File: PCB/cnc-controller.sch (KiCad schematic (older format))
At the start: 12 parts

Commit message: キーマトリクスとLEDの回路図を作成
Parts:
- added R?: 10k, symbol Device:R
- added R?: 500, symbol Device:R
- added SW? (x24): sw_unit, symbol cnc-controller_Library:kailh_chocv1_sw_unit
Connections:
- net labels added: +5VP
- wire segments 65 -> 280
- no-connect marks 12 -> 13
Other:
- moved on the sheet: F?, J?, R?, U?

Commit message: USBのデータ線の保護素子を変更 USB周りの配線を変更及び書き直し
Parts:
- removed D? (x2): 5.1V, symbol Device:D_Zener
- removed R? (x2): 5.1k, symbol Device:R
- added R? (x2): 10k, symbol Device:R
- added R? (x2): 27, symbol Device:R
- added R? (x2): 5.1k, symbol Device:R
- added U?: SN65220, Package_TO_SOT_SMD:SOT-23-6, symbol Power_Protection:SN65220
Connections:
- wire segments 280 -> 290
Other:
- moved on the sheet: F?, J?, R?

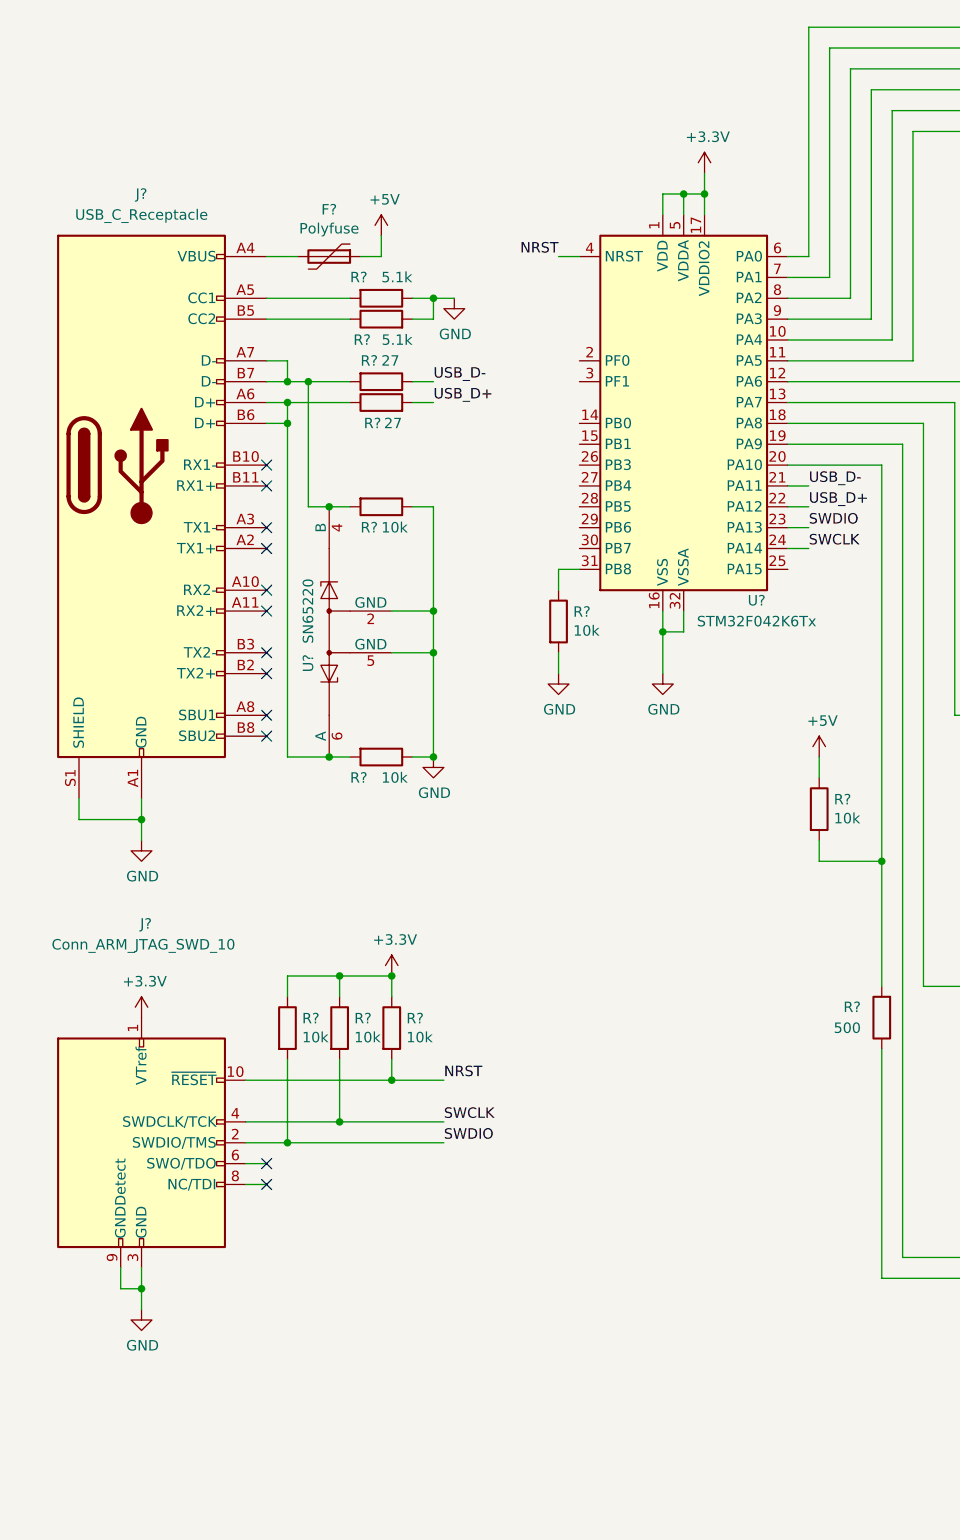
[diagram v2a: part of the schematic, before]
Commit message: 3.3Vレギュレータを追加 マイコンの電源用コンデンサを追加 VBUS付近にPWR_FLAGを追加
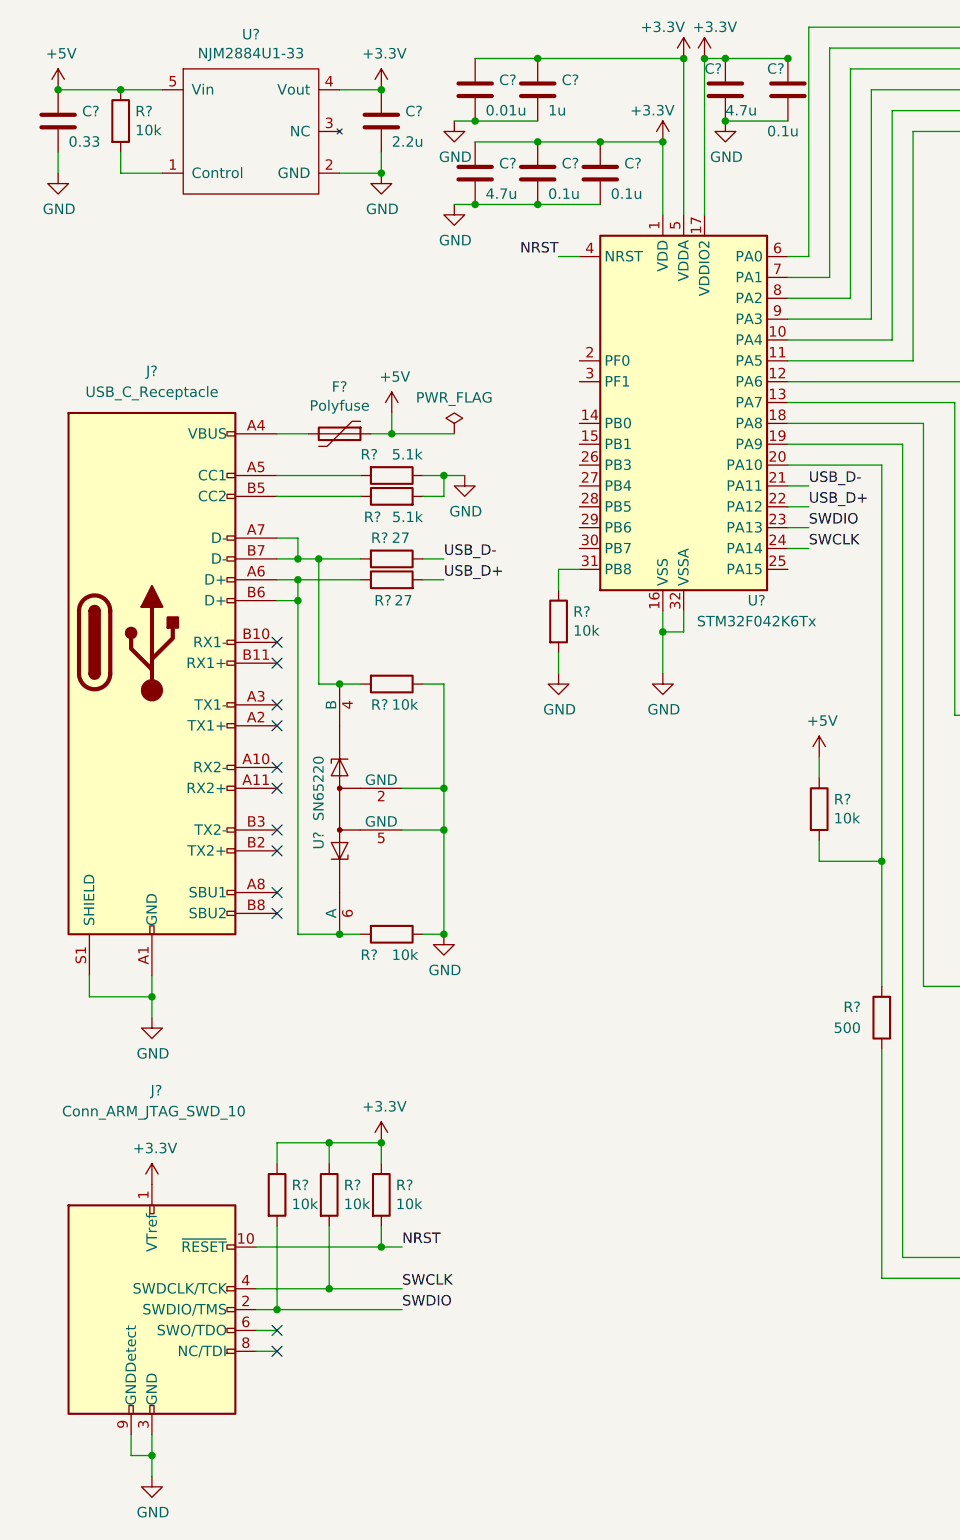
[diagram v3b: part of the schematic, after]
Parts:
- added C?: 0.33, symbol Device:C
- added C?: 2.2u, symbol Device:C
- added C? (x2): 4.7u, symbol Device:C
- added C? (x3): 0.1u, symbol Device:C
- added C?: 0.01u, symbol Device:C
- added C?: 1u, symbol Device:C
- added R?: 10k, symbol Device:R
- added U?: NJM2884U1-33, symbol cnc-controller_Library:NJM2884U1-33
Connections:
- net +3V3: now also C?.1, C?.1, C?.1, C?.1, C?.1, C?.1, C?.1, C?.1, U?.4 (Vout)
- net +5V: now also C?.1, R?.1, U?.5 (Vin)
- net GND: now also C?.2, C?.2, C?.2, C?.2, C?.2, C?.2, C?.2, C?.2, C?.2, U?.2 (GND)
- new net: R?.2, U?.1 (Control)
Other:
- moved on the sheet: F?, J?, R?, U?

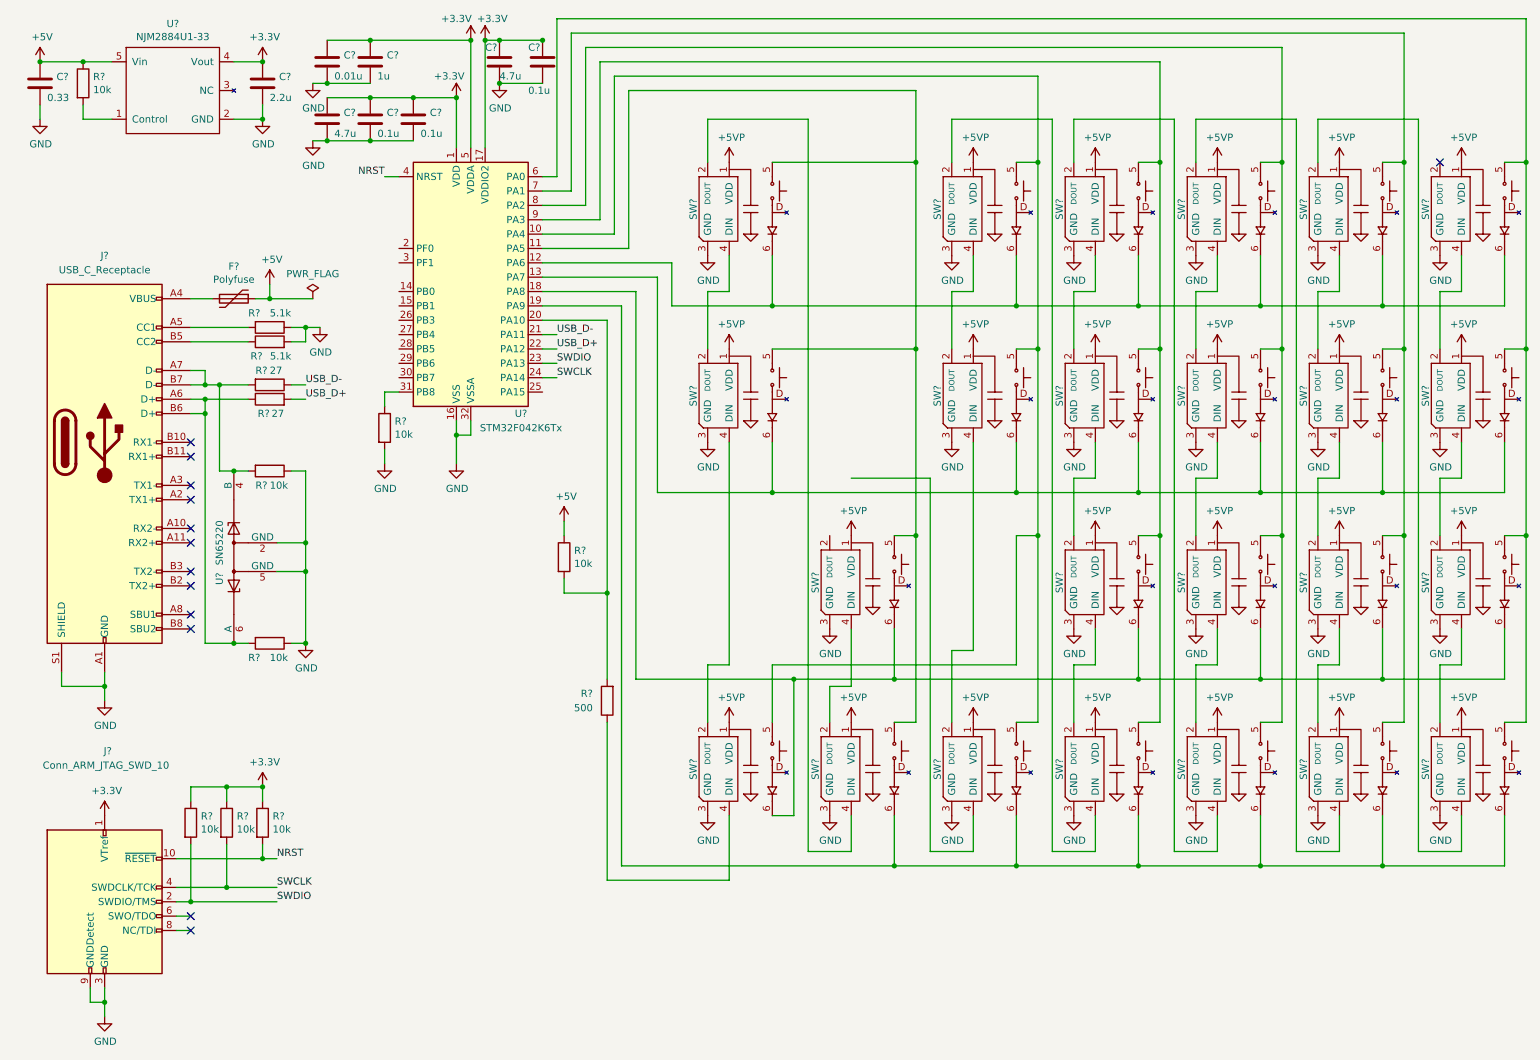
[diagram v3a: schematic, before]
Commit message: キーマトリクスにプルダウン抵抗を追加 LED電源用スイッチの回路を追加
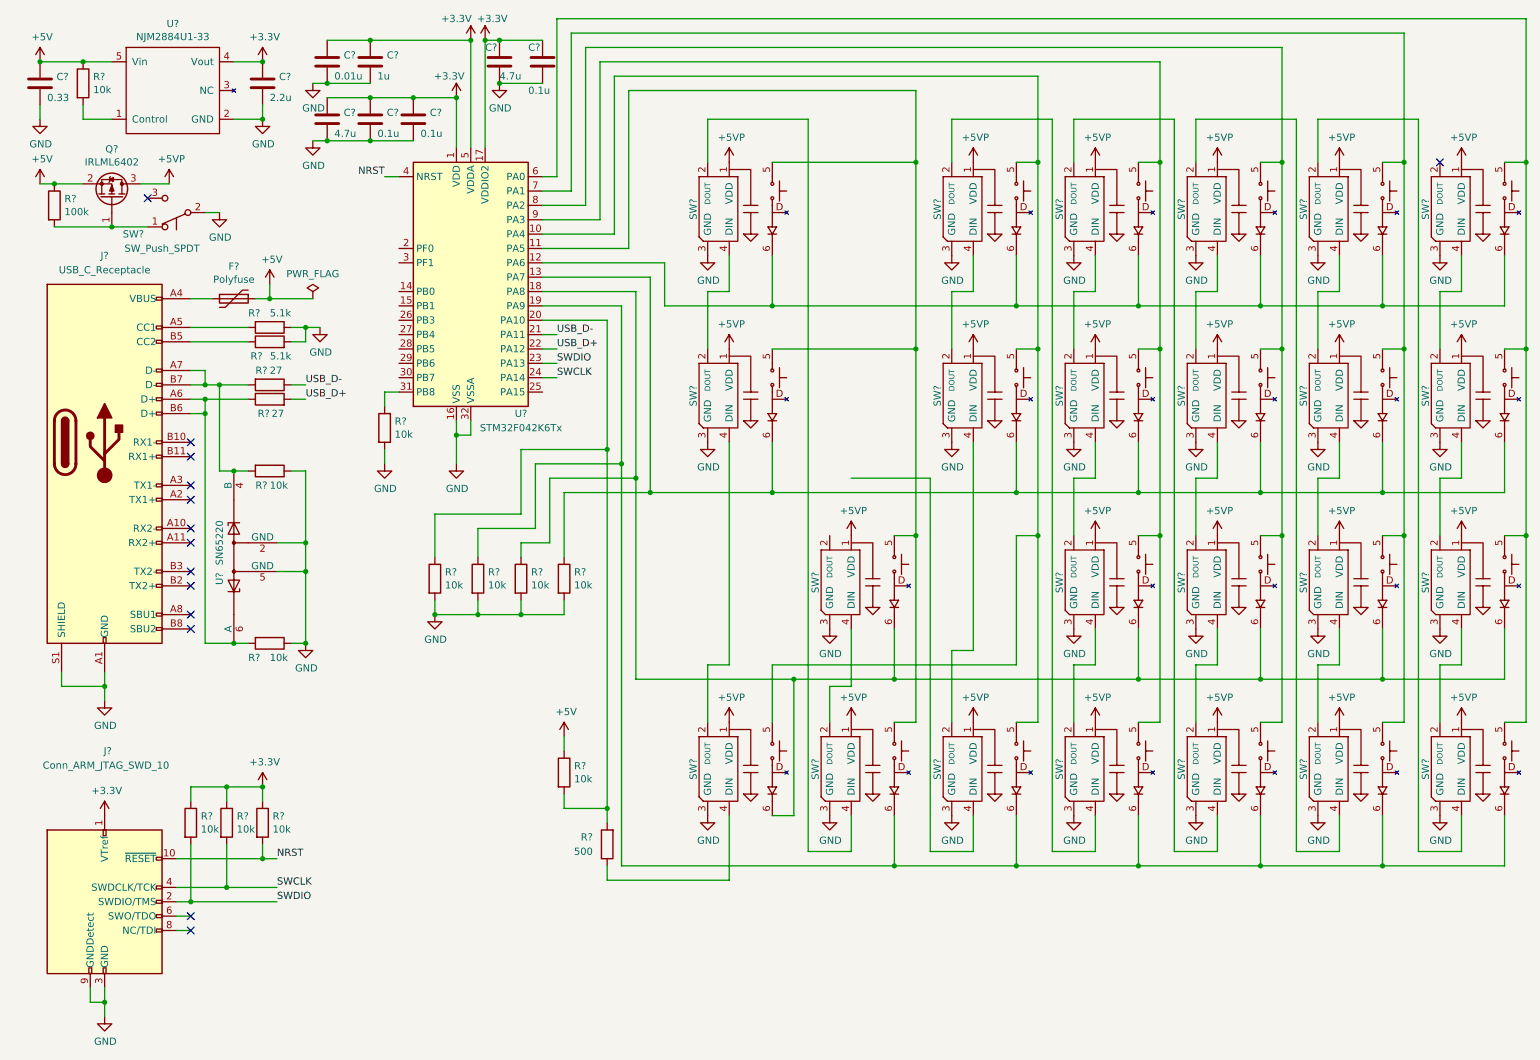
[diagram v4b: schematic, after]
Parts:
- added Q?: IRLML6402, symbol Device:Q_PMOS_GSD
- added R? (x4): 10k, symbol Device:R
- added R?: 100k, symbol Device:R
- added SW?: SW_Push_SPDT, symbol Switch:SW_Push_SPDT
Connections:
- net +5V: now also Q?.2 (S), R?.1
- net +5VP: now also Q?.3 (D)
- net GND: now also R?.2, R?.2, R?.2, R?.2, SW?.2 (B)
- net at SW?.6, SW?.6, SW?.6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: now also R?.1 (x3)
- net at R?.2, R?.2, U?.20 (PA10): now also R?.1
- new net: Q?.1 (G), R?.2, SW?.1 (A)
- no-connect marks 13 -> 14
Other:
- moved on the sheet: R?

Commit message: リセットスイッチを追加 キーユニットに作図補助線を追加 スイッチ用のフットプリント2つ(トグルスイッチとプッシュスイッチ)用を作成
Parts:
- added C5: 0.1u, symbol Device:C
- added J3: Conn_01x04, symbol Connector_Generic:Conn_01x04
- added J4: Conn_01x03, symbol Connector_Generic:Conn_01x03
- added SW2: SW_Push, symbol Switch:SW_Push
- SW1: renamed from SW?; value SW_Push_SPDT -> SK-12D11VG3
- gave numbers to parts that had none: 58
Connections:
- net GND: now also C5.2, J3.3 (Pin_3), J4.1 (Pin_1), SW2.1
- net NRST: now also C5.1, J3.1 (Pin_1), SW2.2
- net SWCLK: now also J3.4 (Pin_4)
- net SWDIO: now also J3.2 (Pin_2)
- net at U3.29 (PB6): now also J4.3 (Pin_3)
- net at U3.30 (PB7): now also J4.2 (Pin_2)
- net at SW6.2 (DOUT): now also SW10.4 (DIN)
- no-connect marks 14 -> 22
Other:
- moved on the sheet: R12

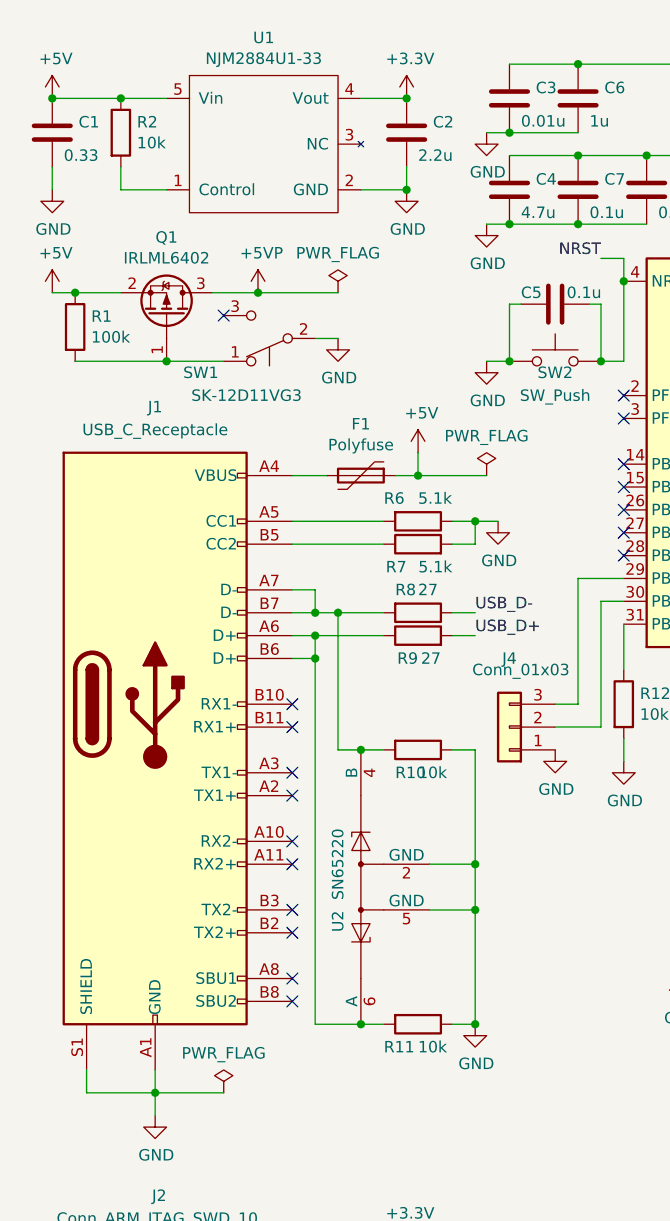
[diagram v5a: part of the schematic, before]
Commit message: フットプリントの関連付けを行った
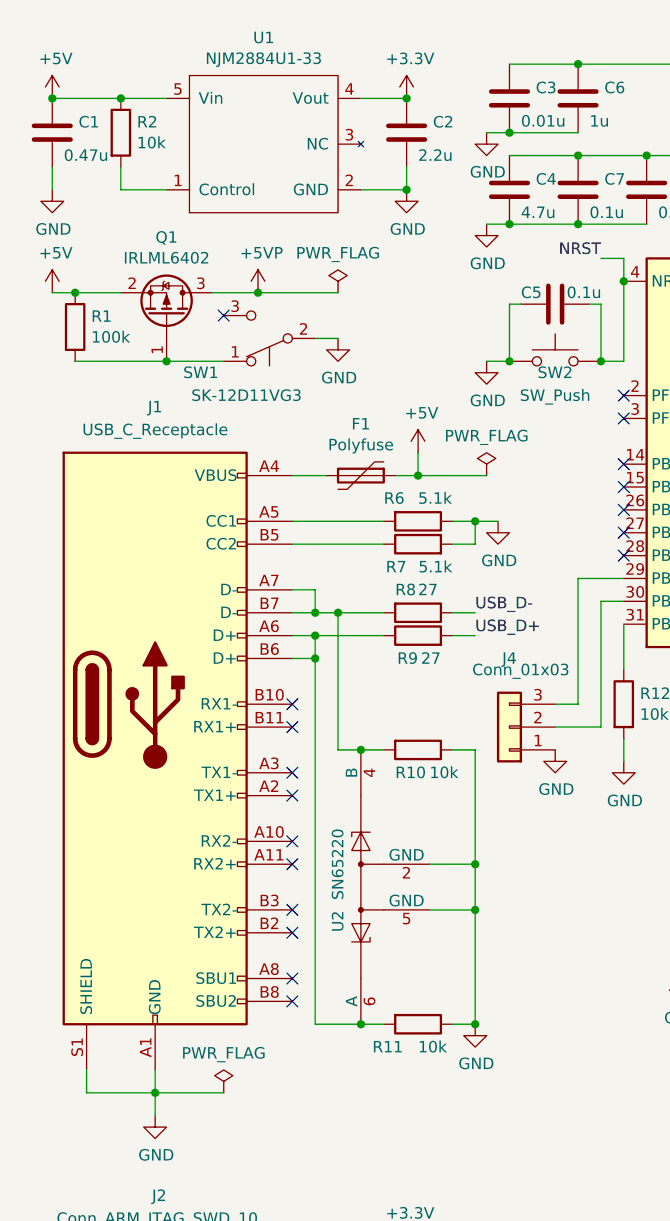
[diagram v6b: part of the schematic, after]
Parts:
- C1: value 0.33 -> 0.47u; footprint (none) -> Capacitor_SMD:C_0402_1005Metric_Pad0.74x0.62mm_HandSolder
- C10, C3, C4, C5, C6, C7, C8, C9: footprint (none) -> Capacitor_SMD:C_0603_1608Metric_Pad1.08x0.95mm_HandSolder
- C2: footprint (none) -> Capacitor_SMD:C_0805_2012Metric_Pad1.18x1.45mm_HandSolder
- F1: footprint (none) -> Fuse:Fuse_0603_1608Metric_Pad1.05x0.95mm_HandSolder
- J1: footprint (none) -> cnc-controller_Library:USBC_5077CR-16-SMC2-BK-TR
- J2: footprint (none) -> Connector_PinHeader_1.27mm:PinHeader_2x05_P1.27mm_Vertical
- J3: footprint (none) -> Connector_PinHeader_2.54mm:PinHeader_1x04_P2.54mm_Vertical
- J4: footprint (none) -> Connector_PinHeader_2.54mm:PinHeader_1x03_P2.54mm_Vertical
- Q1: footprint (none) -> Package_TO_SOT_SMD:SOT-23
- R1, R10, R11, R12, R13, R14, R15, R16, R17, R18, R2, R3, R4, R5, R6, R7, R8, R9: footprint (none) -> Resistor_SMD:R_0603_1608Metric_Pad0.98x0.95mm_HandSolder
- SW1: footprint (none) -> cnc-controller_Library:SW_SK-12D11VG3
- SW10, SW11, SW12, SW13, SW14, SW15, SW16, SW17, SW18, SW19, SW20, SW21, SW22, SW23, SW24, SW25, SW26, SW3, SW4, SW5, SW6, SW7, SW8, SW9: footprint (none) -> cnc-controller_Library:kailh_chocv1_unit
- SW2: footprint (none) -> cnc-controller_Library:SW_TVBP06-B043CB-B
- U1: footprint (none) -> Package_TO_SOT_SMD:SOT-89-5_Handsoldering
